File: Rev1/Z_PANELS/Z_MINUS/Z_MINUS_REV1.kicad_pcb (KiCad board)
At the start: 2 copper layers, 98 x 98 mm, 62 parts, among them IC1 LTC4316IDD#PBF, IC2 SM141K08TFV, IC3 SM141K04TFV, IC4 SM141K04TFV, IC5 SM141K04TFV, IC6 SM141K08TFV, J1 F3311A7H121014E200, Q1 BSS138, Q2 BSS138, Q3 MBT2222ADW1T1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

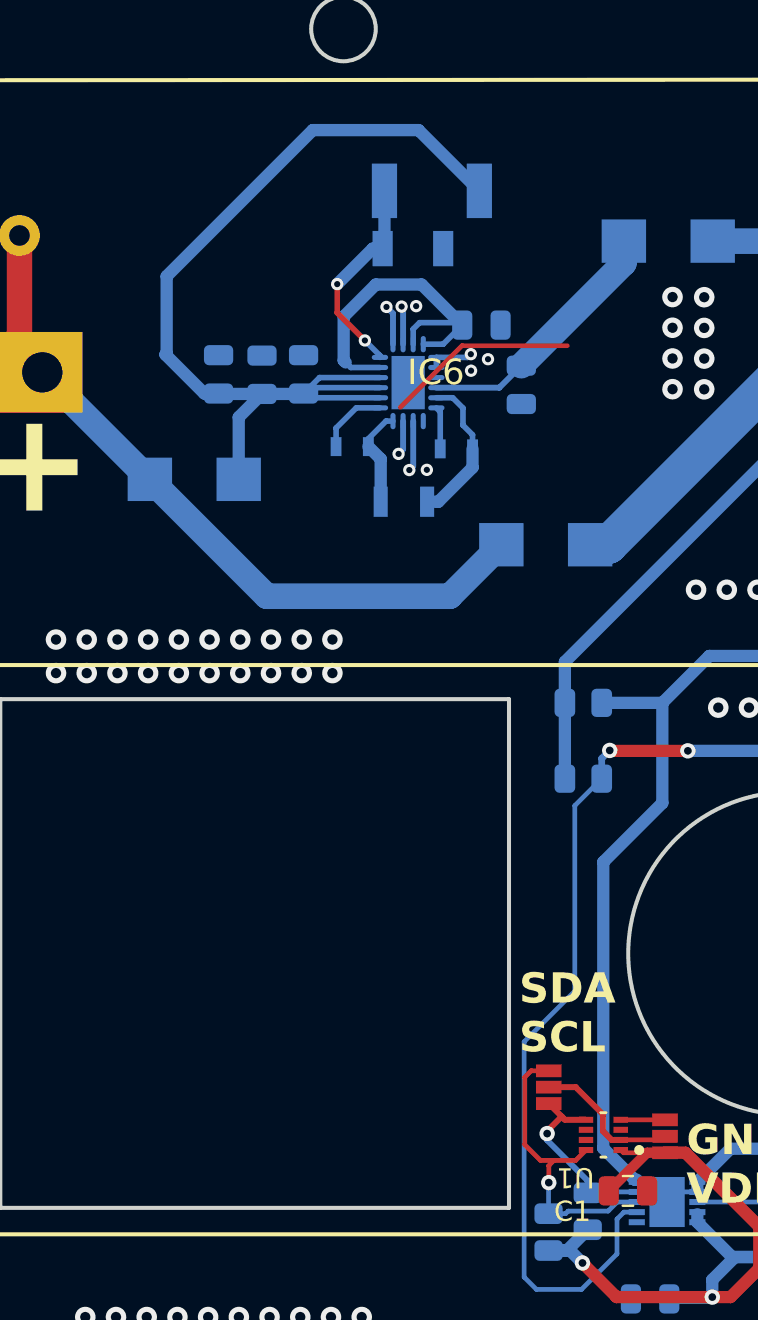
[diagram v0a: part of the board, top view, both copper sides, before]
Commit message: updated cap footprint
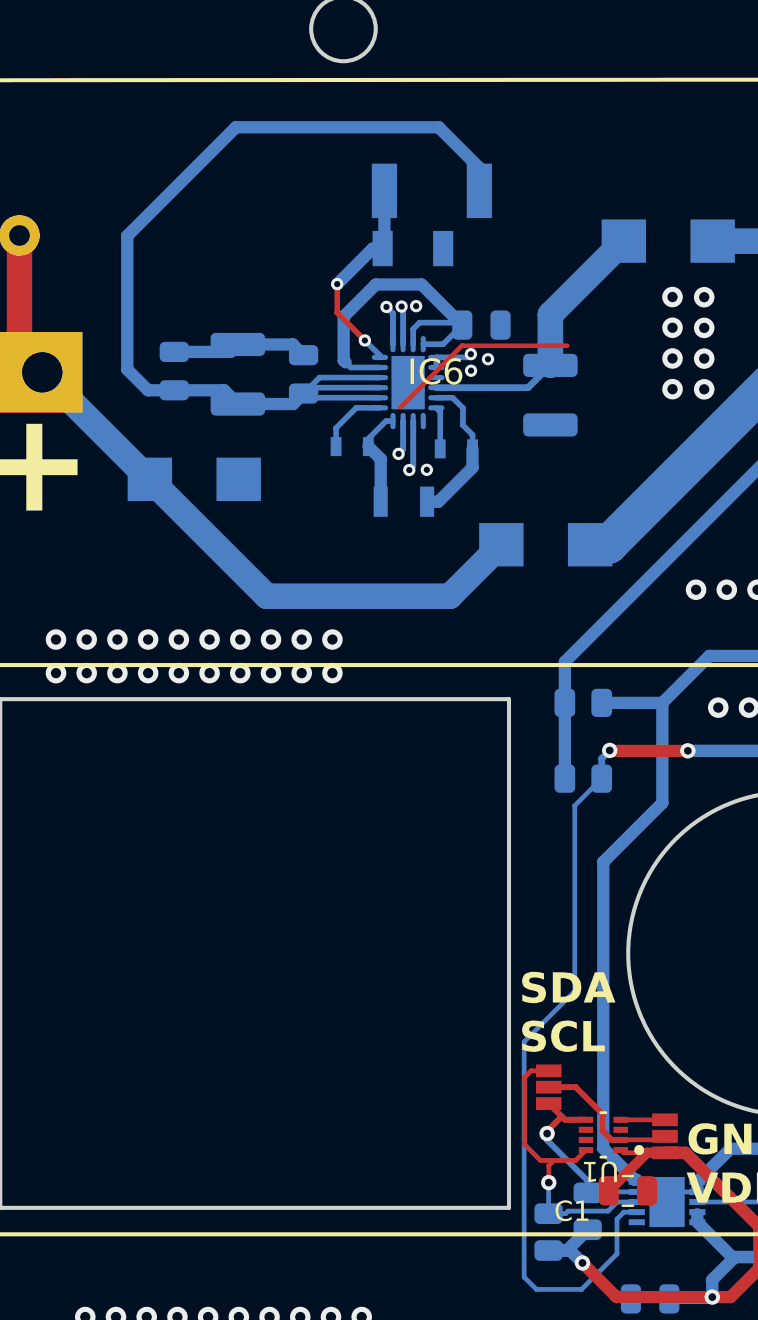
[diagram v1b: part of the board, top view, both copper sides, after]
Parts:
- C11, C6: footprint Capacitor_SMD:C_0805_2012Metric -> Capacitor_SMD:C_1210_3225Metric
- moved C5 2.20 mm to (106.1, 72.7)
- moved C11 1.53 mm to (124.7, 73.9)
- moved C6 1.19 mm to (109.2, 72.9)
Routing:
- net GND: track 36.4 -> 43.2 mm
- net Net-(U2-PVIN): track 47.9 -> 49.8 mm
- net Net-(U2-VOUT): track 12.9 -> 13.8 mm

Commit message: final z minus nischal signioff
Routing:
- net GND: track 43.2 -> 36.4 mm
- net Net-(U2-PVIN): track 49.8 -> 53.5 mm
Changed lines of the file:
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@@
   (segment (start 120.61 72.06) (end 120.77 71.9) (width 0.2794) (layer "B.Cu") (net 2))
   (segment (start 130.99 113.4) (end 130.49 113.9) (width 0.23495) (layer "B.Cu") (net 2))
-  (segment (start 108.86 71.79) (end 109.23 71.42) (width 0.6096) (layer "B.Cu") (net 2))
   (segment (start 116.913499 69.883499) (end 116.59 69.56) (width 0.29337) (layer "B.Cu") (net 2))
   (segment (start 131.99 112.9) (end 131.99 113.2928) (width 0.6096) (layer "B.Cu") (net 2))
   (segment (start 167.595 76.9) (end 164.07 76.9) (width 0.23495) (layer "B.Cu") (net 2))
-  (segment (start 106.08 71.79) (end 108.86 71.79) (width 0.6096) (layer "B.Cu") (net 2))
   (segment (start 119.0605 72.559999) (end 119.0605 72.06) (width 0.2794) (layer "B.Cu") (net 2))
   (segment (start 136.481952 111.26) (end 133.63 111.26) (width 0.6096) (layer "B.Cu") (net 2))
@@
   (segment (start 164.07 76.9) (end 163.25 76.08) (width 0.23495) (layer "B.Cu") (net 2))
   (segment (start 116.913499 71.405) (end 116.913499 69.883499) (width 0.29337) (layer "B.Cu") (net 2))
-  (segment (start 111.9535 71.42) (end 112.4835 71.95) (width 0.6096) (layer "B.Cu") (net 2))
-  (segment (start 109.23 71.42) (end 111.9535 71.42) (width 0.6096) (layer "B.Cu") (net 2))
   (segment (start 117.9135 75.215) (end 117.9135 77.4465) (width 0.29337) (layer "B.Cu") (net 2))
   (segment (start 166.84 80.4) (end 167.595 80.4) (width 0.23495) (layer "B.Cu") (net 2))
@@
   (segment (start 116.2665 73.56) (end 112.7735 73.56) (width 0.2794) (layer "B.Cu") (net 4))
   (segment (start 121.19 63.81) (end 121.19 62.67) (width 0.6096) (layer "B.Cu") (net 4))
+  (segment (start 109.27 78.1) (end 109.27 74.41) (width 1.27) (layer "B.Cu") (net 4))
   (segment (start 112.7735 73.56) (end 112.4835 73.85) (width 0.2794) (layer "B.Cu") (net 4))
   (segment (start 121.19 62.67) (end 119.18 60.66) (width 0.6096) (layer "B.Cu") (net 4))
+  (segment (start 109.27 74.41) (end 109.23 74.37) (width 1.27) (layer "B.Cu") (net 4))
   (segment (start 111.9635 74.37) (end 112.4835 73.85) (width 0.6096) (layer "B.Cu") (net 4))
   (segment (start 104.78 73.69) (end 106.08 73.69) (width 0.6096) (layer "B.Cu") (net 4))
@@
     (connect_pads (clearance 0.254))
     (min_thickness 0.2286) (filled_areas_thickness no)
-    (fill yes (thermal_gap 0.635) (thermal_bridge_width 0.508))
+    (fill yes (thermal_gap 0.254) (thermal_bridge_width 0.508))
     (polygon
       (pts
